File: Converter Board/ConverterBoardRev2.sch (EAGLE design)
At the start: 18 parts

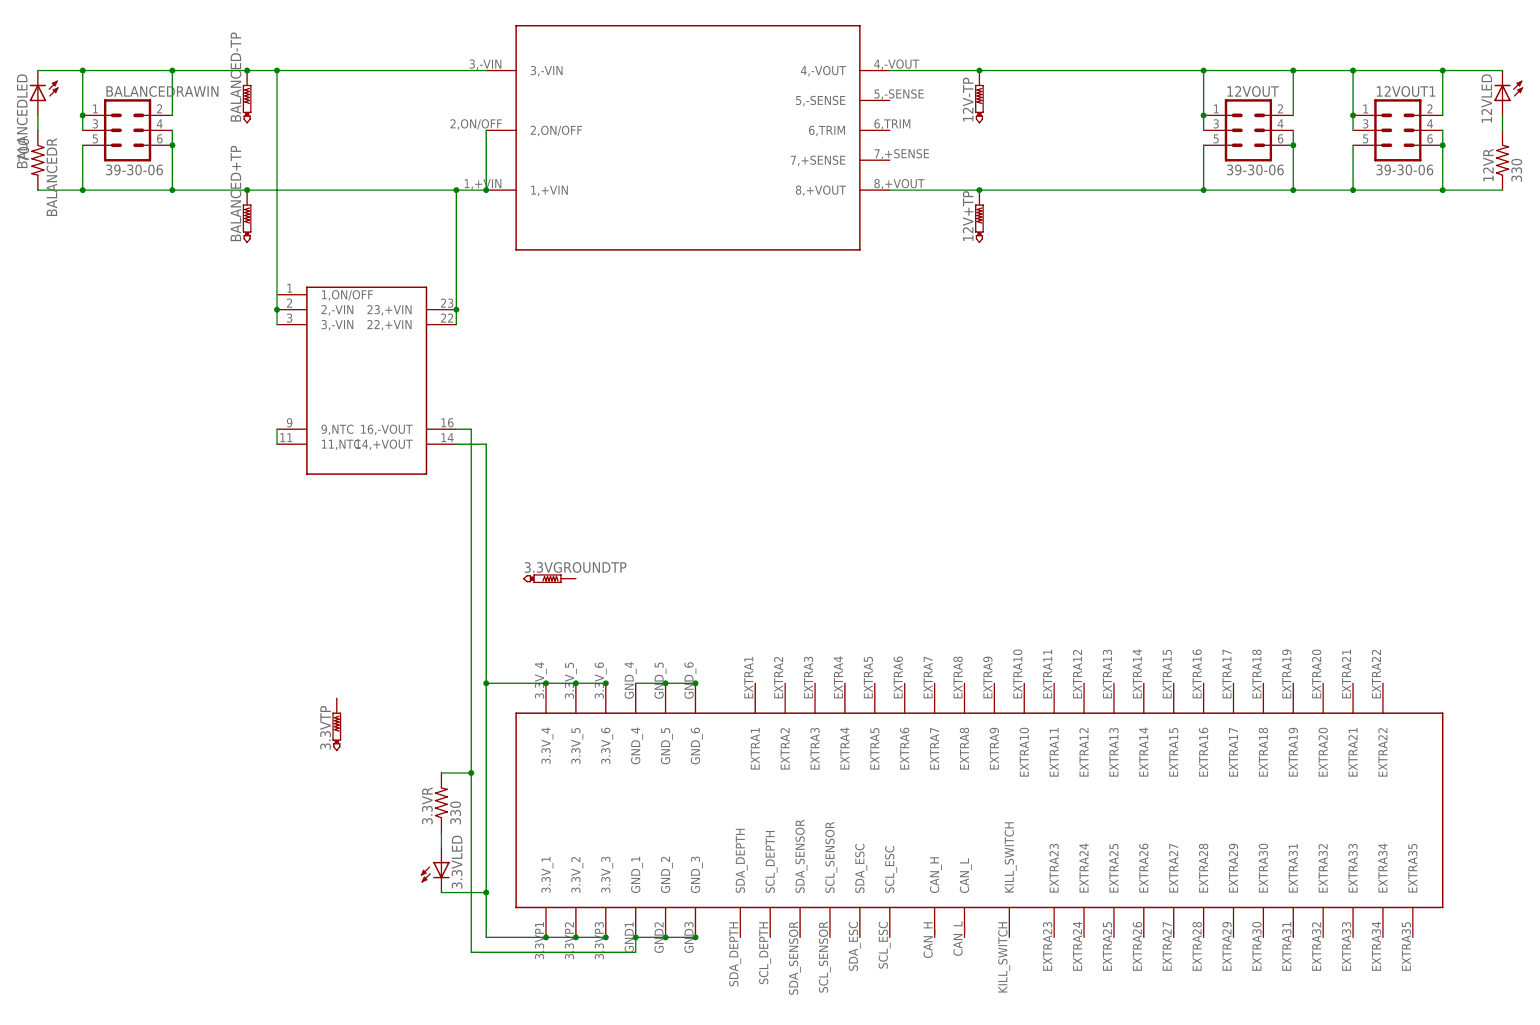
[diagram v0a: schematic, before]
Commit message: Additions to Rev2, added sensors to schematic
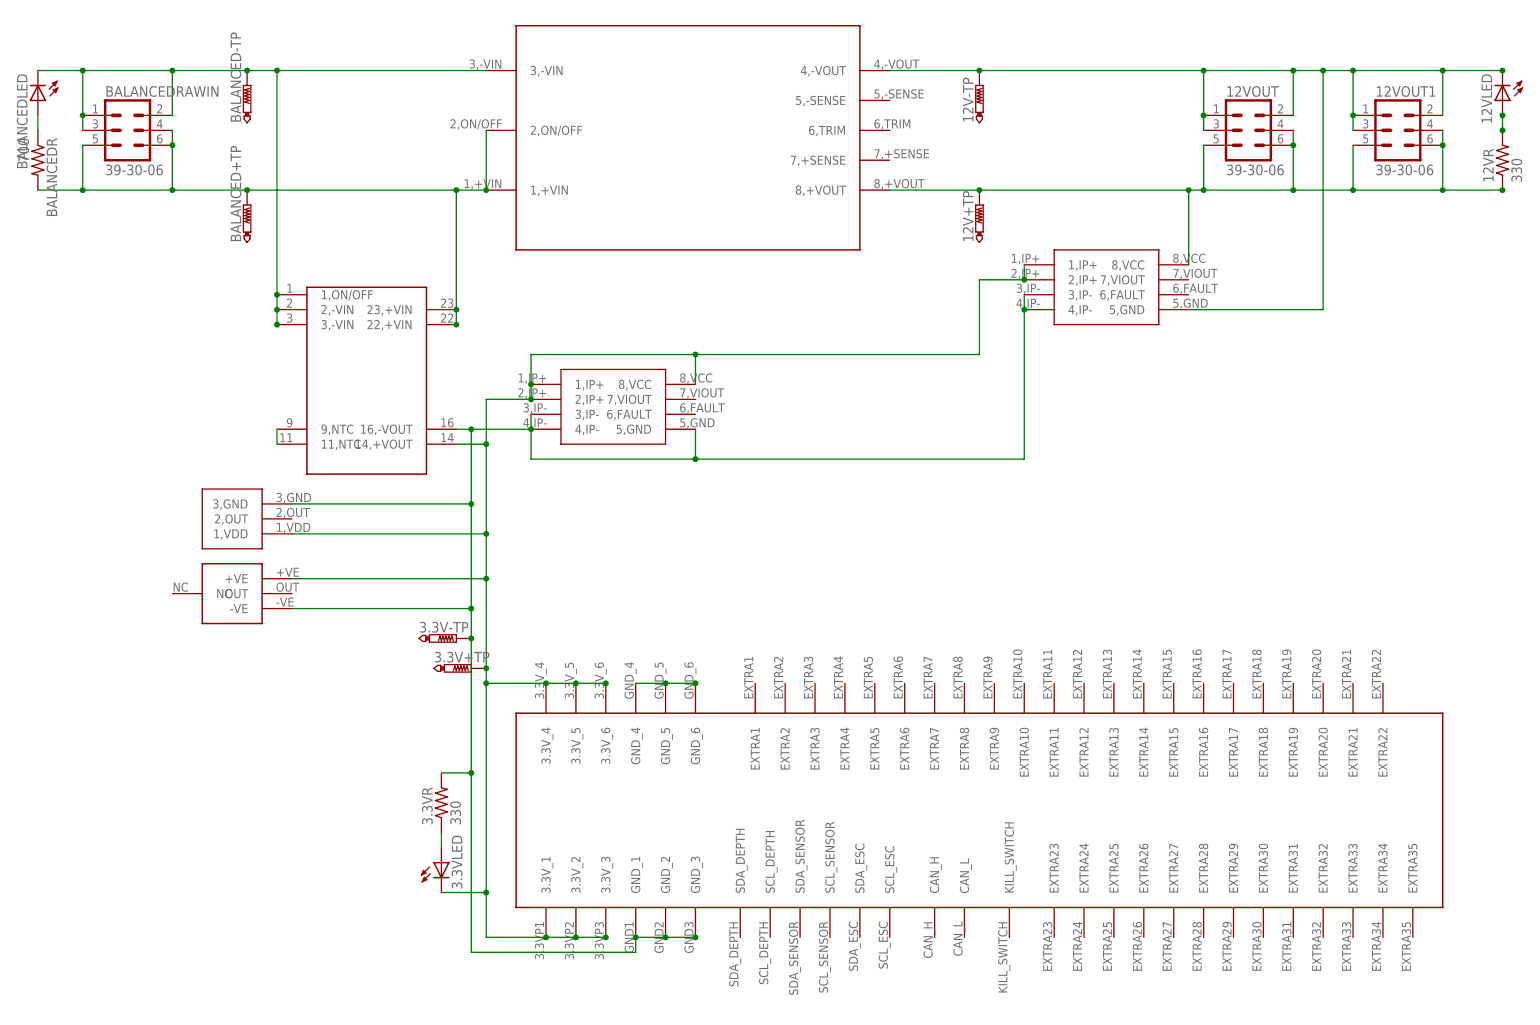
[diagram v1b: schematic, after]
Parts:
- removed 3.3VGROUNDTP, 3.3VTP: PTR1B1,27, testpad:PTR1B1,27
- added 3.3V+TP, 3.3V-TP: PTR1B1,27, testpad:PTR1B1,27
- added U$4, U$5: CURRENTSENS, CurrentSensor:CURRENTSENS
- added U$6: HUMIDITYSENSOR, HumiditySensor:HUMIDITYSENSOR
- added U$7: TEMPSENS, TemperatureSensor:TEMPSENS
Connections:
- net N$5 renamed 3.3VLED
- removed net 3.3V: 3.3VLED.C, U$2.14,+VOUT, U$3.3.3V_1, U$3.3.3V_2, U$3.3.3V_3, U$3.3.3V_4, U$3.3.3V_5, U$3.3.3V_6
- removed net 3.3VGROUND: 3.3VR.2, U$2.16,-VOUT, U$3.GND_1, U$3.GND_2, U$3.GND_3
- removed net N$2: 12V+TP.TP, 12VOUT.4, 12VOUT.5, 12VOUT.6, 12VOUT1.4, 12VOUT1.5, 12VOUT1.6, 12VR.1, U$1.8,+VOUT
- removed net N$3: 12V-TP.TP, 12VLED.C, 12VOUT.1, 12VOUT.2, 12VOUT.3, 12VOUT1.1, 12VOUT1.2, 12VOUT1.3, U$1.4,-VOUT
- new net 12V+: 12V+TP.TP, 12VOUT.4, 12VOUT.5, 12VOUT.6, 12VOUT1.4, 12VOUT1.5, 12VOUT1.6, 12VR.1, U$1.8,+VOUT, U$4.8,VCC
- new net 12V-: 12V-TP.TP, 12VLED.C, 12VOUT.1, 12VOUT.2, 12VOUT.3, 12VOUT1.1, 12VOUT1.2, 12VOUT1.3, U$1.4,-VOUT, U$4.5,GND
- new net 3.3V+: 3.3V+TP.TP, 3.3VLED.C, U$2.14,+VOUT, U$3.3.3V_1, U$3.3.3V_2, U$3.3.3V_3, U$3.3.3V_4, U$3.3.3V_5, U$3.3.3V_6, U$4.1,IP+, U$4.2,IP+, U$5.1,IP+, U$5.2,IP+, U$5.8,VCC, U$6.+VE, U$7.1,VDD
- new net 3.3V-: 3.3V-TP.TP, 3.3VR.2, U$2.16,-VOUT, U$3.GND_1, U$3.GND_2, U$3.GND_3, U$4.3,IP-, U$4.4,IP-, U$5.3,IP-, U$5.4,IP-, U$5.5,GND, U$6.-VE, U$7.3,GND
- net BALANCED-: now also U$2.1,ON/OFF
